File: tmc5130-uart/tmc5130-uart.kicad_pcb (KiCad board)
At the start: 4 copper layers, 40 x 40 mm, 103 parts, among them J1301 Connector_USB_C_Receptacle, J301 Molex_Pico-SPOX_Horizontal, J302 Molex_Pico-Lock-PLUS_Vertical, J401 Molex_Pico-SPOX_Horizontal, J402 Molex_Pico-Clasp_Horizontal, M301 Fan_5VDC_25x25x8mm, Q301 MOSFET-N-CH, SW1301 Switch_Tactile_SPST-NO_SMT_Si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, U1001 BUK7D36-60EX, U1101 BUK7D36-60EX, U1201 BUK7D36-60EX, U1301 Linear_3.3V_1A, U1302 MCU_RP2040, U1303 Memory_Flash_W25Q128JVZPIQ, U301 Switching_5V_500mA, U302 Linear_3.3V_1A, U401 TMC5160A-WA, U402 MAX6816, U501 BUK7D36-60EX, U601 BUK7D36-60EX, U701 BUK7D36-60EX, U801 BUK7D36-60EX, U901 BUK7D36-60EX, X401 16MHz, Y1301 Crystal_12MHz

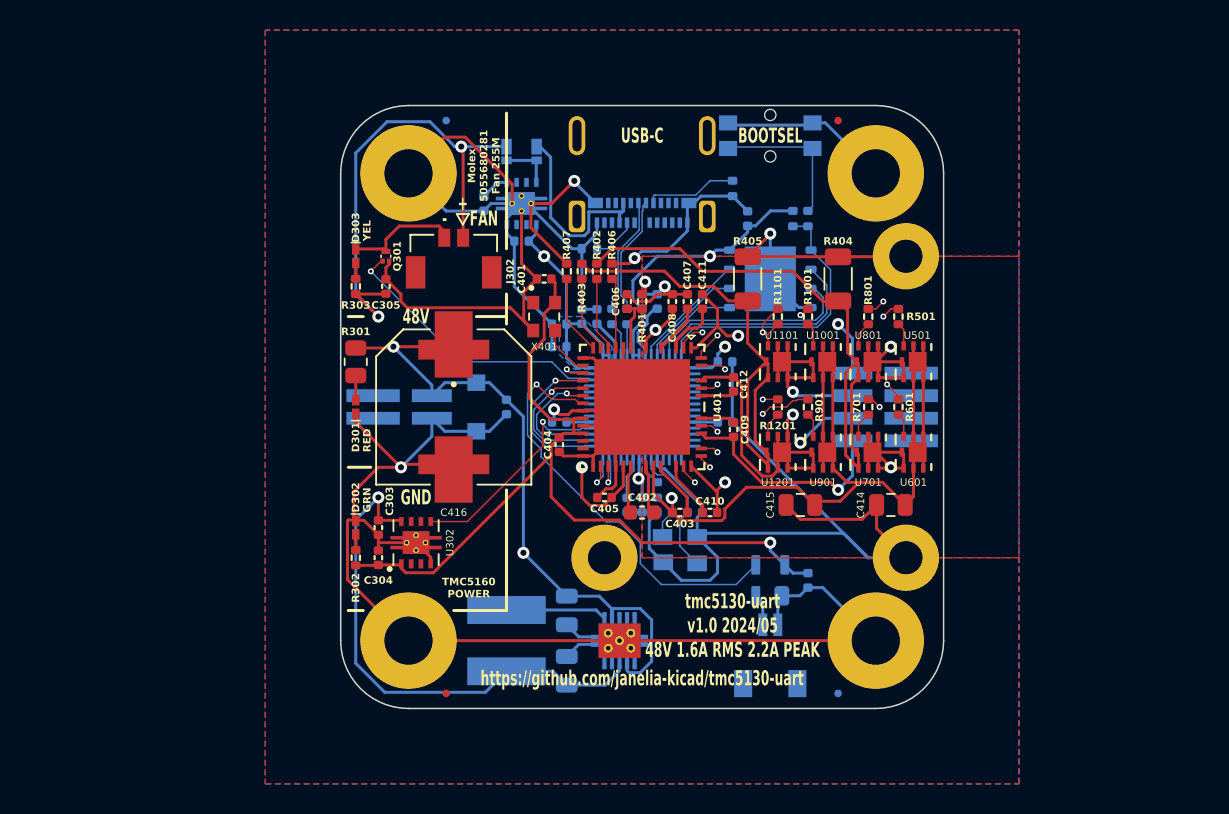
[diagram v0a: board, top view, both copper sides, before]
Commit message: Add components from jlcpcb
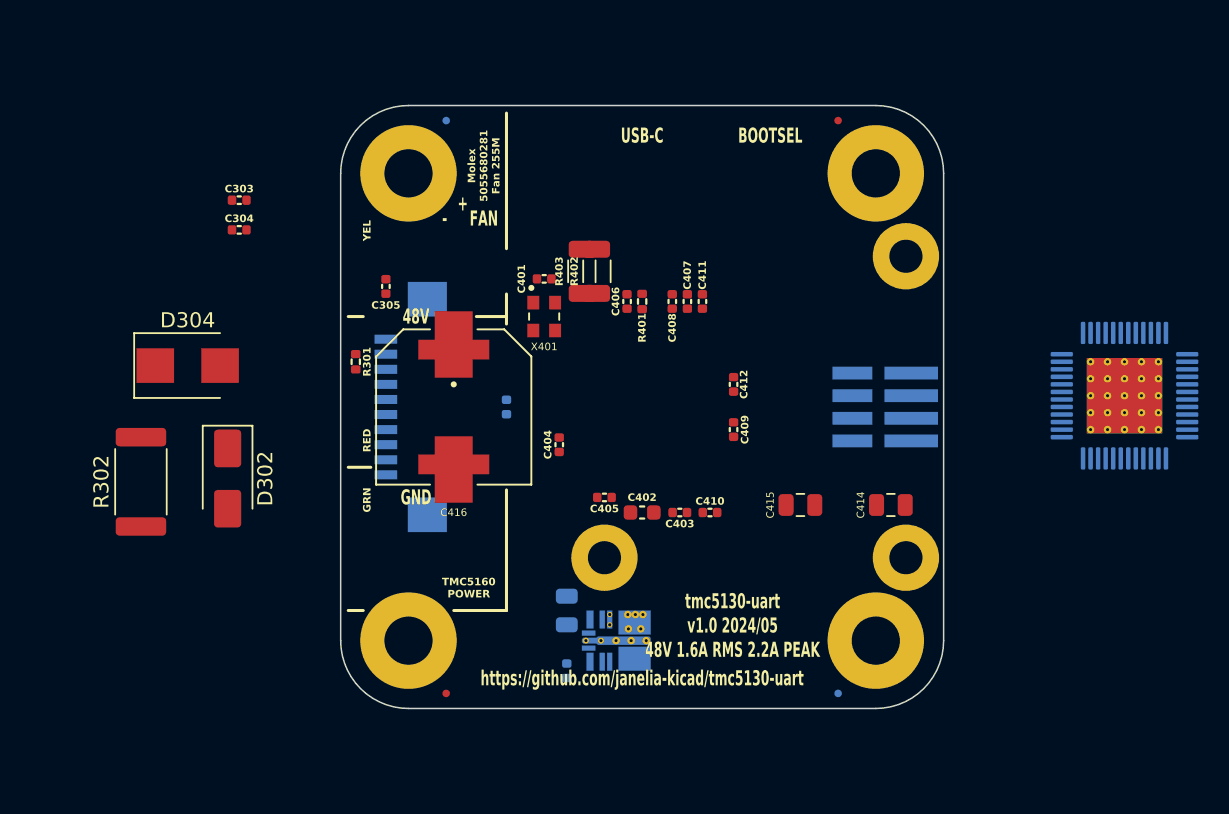
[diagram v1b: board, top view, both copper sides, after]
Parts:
- removed C1301, C1302: 1uF_25V, Janelia:C_0402_1005Metric
- removed C1303, C1311: 1uF_35V, Janelia:C_0402_1005Metric
- removed C1304, C1305, C1306, C1307, C1308, C1309, C1310, C1312, C1313, C1314, C417: 0.1uF_100V, Janelia:C_0402_1005Metric
- removed C1315, C1316: 15pF_25V, Janelia:C_0402_1005Metric
- removed D1301, D1302: D_SCHOTTKY_40V_2A, Janelia:CR_DSN2_152AB-C_OSI
- removed D301: LED_RED, Janelia:LED_0402-1005_KNB
- removed D303: LED_YEL, Janelia:LED_0402-1005_KNB
- removed D401: D_Zener_48V_2.6A, Janelia:SMFSeries_LTF
- removed J1301: Connector_USB_C_Receptacle, Janelia:USB_C_Receptacle_Amphenol_10152803-00011LF
- removed J302: Molex_Pico-Lock-PLUS_Vertical, Janelia:Molex_Micro-Lock-PLUS-505568_1x02_P1.25mm_Vertical
- removed J402: Molex_Pico-Clasp_Horizontal, Janelia:Molex_Pico-Clasp-501568_1x02_P1mm_Horizontal
- removed L301: 150uH_553mA, Janelia:IND_CB_SD25
- removed Q301: MOSFET-N-CH, Janelia:XFDFN-3
- removed R1001, R1101, R1201, R501, R601, R701, R801, R901: 15, Janelia:R_0402_1005Metric
- removed R1301: 10.0k, Janelia:R_0402_1005Metric
- removed R1302, R1303: 5.1k, Janelia:R_0402_1005Metric
- removed R1304, R1305: 27, Janelia:R_0402_1005Metric
- removed R1306, R1307: 1k, Janelia:R_0402_1005Metric
- removed R303: 249, Janelia:R_0402_1005Metric
- removed R404, R405: 0.15, Janelia:R_1206_3216Metric
- removed R406, R407: 47, Janelia:R_0402_1005Metric
- removed SW1301: Switch_Tactile_SPST-NO_SMT_Side, Janelia:SMT_1045822_WRE
- removed U1001, U1101, U1201, U501, U601, U701, U801, U901: BUK7D36-60EX, Janelia:BUK7D3660EX_NEX
- removed U1301, U302: Linear_3.3V_1A, Janelia:TPS737Q1
- removed U1302: MCU_RP2040, Janelia:QFN-56-1EP_7x7mm_P0.4mm_EP3.2x3.2mm
- removed U1303: Memory_Flash_W25Q128JVZPIQ, Janelia:WSON-8-1EP_6x5mm_P1.27mm_EP3.4x4.3mm
- removed U401: TMC5160A-WA, Janelia:21-100593_ADI
- removed Y1301: Crystal_12MHz, Janelia:Crystal_SMD_Abracon_ABM8-4Pin_3.2x2.5mm
- added D304: D, Janelia:D_SMB, F.Cu at (122.2, 98.8)
- C301: value 2.2uF_100V -> 1uF_100V
- C302: value 47uF_10V -> 1uF_25V; footprint Janelia:C_0805_2012Metric -> Janelia:C_0402_1005Metric
- C304: value 1uF_25V -> 0.1uF_100V
- D302: value LED_GRN -> D_Zener_47V_1W; footprint Janelia:LED_0402-1005_KNB -> Janelia:D_SMA
- J301: value Molex_Pico-SPOX_Horizontal -> FFC_P1mm_BOT_RA_SMD; footprint Janelia:Molex_Pico-SPOX-87438_1x02-P1.5mm_Horizontal -> Janelia:CONN_C2914097
- R301: value 2.32k -> 100k; footprint Janelia:R_0805_2012Metric -> Janelia:R_0402_1005Metric
- R302: value 64.9 -> 0.24; footprint Janelia:R_0402_1005Metric -> Janelia:R_2512_6332Metric
- R402, R403: value 47 -> 0.12; footprint Janelia:R_0402_1005Metric -> Janelia:R_1206_3216Metric
- U301: value Switching_5V_500mA -> TPSM365R6V5RDNR; footprint Janelia:Texas_S-PVSON-N10_ThermalVias -> Janelia:RDN0011A-MFG
- U402: value MAX6816 -> TMC5130A-TA; footprint Janelia:SOT192P237X122-4N -> Janelia:TQFP-48-1EP_7x7mm_P0.5mm_EP5x5mm_ThermalVias
- moved U402 26.5 mm to (184.4, 100.8)
- moved C304 23.6 mm to (125.7, 89.8), turned to 0 degrees
- moved C303 23.6 mm to (125.7, 87.9), turned to 0 degrees
- moved R302 15.1 mm to (119.2, 106.6)
- moved D302 9.10 mm to (124.9, 106.3)
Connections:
- net /tmc5160/BMA1 renamed /tmc5130/BMA1
- net /tmc5160/BMA2 renamed /tmc5130/BMA2
- net /tmc5160/BMB1 renamed /tmc5130/BMB1
- net /tmc5160/BMB2 renamed /tmc5130/BMB2
- C301 pad 1: /VM -> unconnected-(C301-Pad1)
- C301 pad 2: /GND -> unconnected-(C301-Pad2)
- C302 pad 1: /+5V -> unconnected-(C302-Pad1)
- C302 pad 2: /GND -> unconnected-(C302-Pad2)
- C303 pad 1: /+5V -> unconnected-(C303-Pad1)
- C303 pad 2: /GND -> unconnected-(C303-Pad2)
- C304 pad 1: /VIO -> unconnected-(C304-Pad1)
- C304 pad 2: /GND -> unconnected-(C304-Pad2)
- C305 pad 1: /+5V -> /VIO
- C402 pad 1: /tmc5160/CPO -> /tmc5130/CPO
- C402 pad 2: /tmc5160/CPI -> /tmc5130/CPI
- C403 pad 2: /tmc5160/VCP -> /tmc5130/VCP
- C405 pad 1: /tmc5160/VCC -> /tmc5130/VCC
- C406 pad 1: /tmc5160/5VOUT -> /tmc5130/5VOUT
- C407 pad 1: /tmc5160/12VOUT -> /tmc5130/12VOUT
- C409 pad 1: /tmc5160/CA1 -> /tmc5130/CA1
- C410 pad 1: /tmc5160/CA2 -> /tmc5130/CA2
- C411 pad 1: /tmc5160/CB1 -> /tmc5130/CB1
- C412 pad 1: /tmc5160/CB2 -> /tmc5130/CB2
- D302 pad 1: /GND -> /interface/VBB
- D302 pad 2: /power/LED_GRN+ -> /GND
- J301 pad 1: /GND -> /SWN
- J301 pad 2: /VM -> /SWP
- R301 pad 1: /VM -> unconnected-(R301-Pad1)
- R301 pad 2: /power/LED_RED+ -> unconnected-(R301-Pad2)
- R302 pad 1: /VIO -> /interface/VAA
- R302 pad 2: /power/LED_GRN+ -> /interface/VBB
- R401 pad 1: /tmc5160/VCC -> /tmc5130/VCC
- R401 pad 2: /tmc5160/5VOUT -> /tmc5130/5VOUT
- R402 pad 1: /tmc5160/SRAH -> unconnected-(R402-Pad1)
- R402 pad 2: /tmc5160/SRA -> unconnected-(R402-Pad2)
- R403 pad 1: /tmc5160/SRBH -> unconnected-(R403-Pad1)
- R403 pad 2: /tmc5160/SRB -> unconnected-(R403-Pad2)
- U301 pad 1: /power/SW -> unconnected-(U301-PGOOD-Pad1)
- U301 pad 10: /GND -> unconnected-(U301-GND-Pad10)
- U301 pad 11: /GND -> unconnected-(U301-MODE_SYNC-Pad11)
- U301 pad 2: /VM -> unconnected-(U301-EN-Pad2)
- U301 pad 3: /GND -> unconnected-(U301-VIN-Pad3)
- U301 pad 5: /GND -> unconnected-(U301-SW-Pad5)
- U301 pad 7: /VM -> unconnected-(U301-BOOT-Pad7)
- U301 pad 8: /+5V -> unconnected-(U301-VCC-Pad8)
- U402 pad 2: /tmc5160/REFL -> /tmc5130/CLOCK
- U402 pad 3: /tmc5160/REFL_DEBOUNCED -> /tmc5130/~{CS}
- U402 pad 4: /VIO -> /tmc5130/SCK
- X401 pad 3: /tmc5160/CLOCK -> /tmc5130/CLOCK
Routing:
- net /GND: track 474.9 -> 0.00 mm, vias 6 -> 0
- net /VM: track 133.3 -> 0.00 mm, vias 4 -> 0
- net /rp2040/+3.3V: track 87.1 -> 0.00 mm, vias 4 -> 0
- net /+5V: track 81.3 -> 0.00 mm, vias 3 -> 0
- net /VIO: track 56.5 -> 0.00 mm, vias 1 -> 0
- net /tmc5130/BMA1: track 39.3 -> 0.00 mm, vias 2 -> 0
- net /tmc5160/SRA: track 37.6 -> 0.00 mm
- net /tmc5130/BMB2: track 33.1 -> 0.00 mm, vias 2 -> 0
- net /tmc5130/BMA2: track 32.7 -> 0.00 mm, vias 3 -> 0
- net /tmc5160/SRB: track 32.5 -> 0.00 mm
- net /tmc5160/REFL_DEBOUNCED: track 28.1 -> 0.00 mm, vias 1 -> 0
- net /tmc5130/BMB1: track 27.4 -> 0.00 mm, vias 2 -> 0
- net /tmc5160/VCC: track 21.8 -> 0.00 mm, vias 2 -> 0
- net /rp2040/+1.1V: track 20.7 -> 0.00 mm
- net /tmc5160/LA1: track 20.6 -> 0.00 mm, vias 2 -> 0
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- removed copper zone on B.Cu, net /GND
- removed copper zone on F.Cu, net /GND
- removed copper zone on In1.Cu, net /GND
- removed copper zone on F.Cu, net /VM
- removed copper zone on In2.Cu, net /VM
- removed copper zone on B.Cu, net /rp2040/+1.1V
- removed copper zone on B.Cu, net /rp2040/+3.3V

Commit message: Add components
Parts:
- removed D302: D_Zener_47V_1W, Janelia:D_SMA
- removed D304: D, Janelia:D_SMB
- added C417: 100uF_50V, Janelia:CAP_EEEFTH101XAV, F.Cu at (116.2, 100.3)
- C301: value 1uF_100V -> 3.3uF_50V; footprint Janelia:C_0805_2012Metric -> Janelia:C_1210_3225Metric
- C416: value 220uF_63V -> 100uF_50V; footprint Janelia:CP_Hybrid_EEHZS1H221V -> Janelia:CAP_EEEFTH101XAV
- R302: value 0.24 -> 120; footprint Janelia:R_2512_6332Metric -> Janelia:R_0402_1005Metric
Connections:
- net /tmc5130/DIAG0 renamed /tmc5130/SWN
- net /tmc5130/DIAG1 renamed /tmc5130/SWP
- C301 pad 1: unconnected-(C301-Pad1) -> /VM
- C301 pad 2: unconnected-(C301-Pad2) -> /GND
- C302 pad 1: unconnected-(C302-Pad1) -> /interface/VDD
- C302 pad 2: unconnected-(C302-Pad2) -> /GND
- C303 pad 1: unconnected-(C303-Pad1) -> /VIO
- C303 pad 2: unconnected-(C303-Pad2) -> /GND
- C304 pad 1: unconnected-(C304-Pad1) -> /VM
- C304 pad 2: unconnected-(C304-Pad2) -> /GND
- J301 pad 10: /interface/VAA -> /VM
- J301 pad 7: /interface/VAA -> /VM
- J301 pad 8: /interface/VAA -> /VM
- J301 pad 9: /interface/VAA -> /VM
- R301 pad 1: unconnected-(R301-Pad1) -> /interface/PGOOD
- R301 pad 2: unconnected-(R301-Pad2) -> /VIO
- R302 pad 1: /interface/VAA -> unconnected-(R302-Pad1)
- R302 pad 2: /interface/VBB -> unconnected-(R302-Pad2)
- U301 pad 1: unconnected-(U301-PGOOD-Pad1) -> /interface/PGOOD
- U301 pad 10: unconnected-(U301-GND-Pad10) -> /GND
- U301 pad 11: unconnected-(U301-MODE_SYNC-Pad11) -> /interface/VCC
- U301 pad 2: unconnected-(U301-EN-Pad2) -> /VM
- U301 pad 3: unconnected-(U301-VIN-Pad3) -> /VM
- U301 pad 4: unconnected-(U301-VOUT-Pad4) -> /VIO
- U301 pad 8: unconnected-(U301-VCC-Pad8) -> /interface/VCC
- U301 pad 9: unconnected-(U301-BIAS-Pad9) -> /VIO
- U402 pad 28: unconnected-(U402-SWSEL-Pad28) -> /VIO
- U402 pad 3: /tmc5130/~{CS} -> unconnected-(U402-~{CS}_CFG3-Pad3)
- U402 pad 30: unconnected-(U402-AIN_IREF-Pad30) -> /GND
- U402 pad 4: /tmc5130/SCK -> unconnected-(U402-SCK_CFG2-Pad4)
- U402 pad 5: /tmc5130/MOSI -> unconnected-(U402-SDI_NAI_CFG1-Pad5)
- U402 pad 7: /tmc5130/MISO -> unconnected-(U402-SDO_NAO_CFG0-Pad7)
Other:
- board text removed: "BOOTSEL"
- board text removed: "USB-C"
